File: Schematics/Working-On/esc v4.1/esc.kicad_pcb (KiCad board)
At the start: 4 copper layers, 63.5 x 38 mm, 77 parts, among them IC1 74HCT08BQ,115, IC2 74HCT08BQ,115, J1 AVR-ISP-10, J2 Conn_01x06, J3 Conn_01x06, J4 8730, J5 8730, J6 8730, J7 8730, J8 8730, U1 TLV76750DRVx, U2 ATmega328P-M, U3 DRV8300DRGER

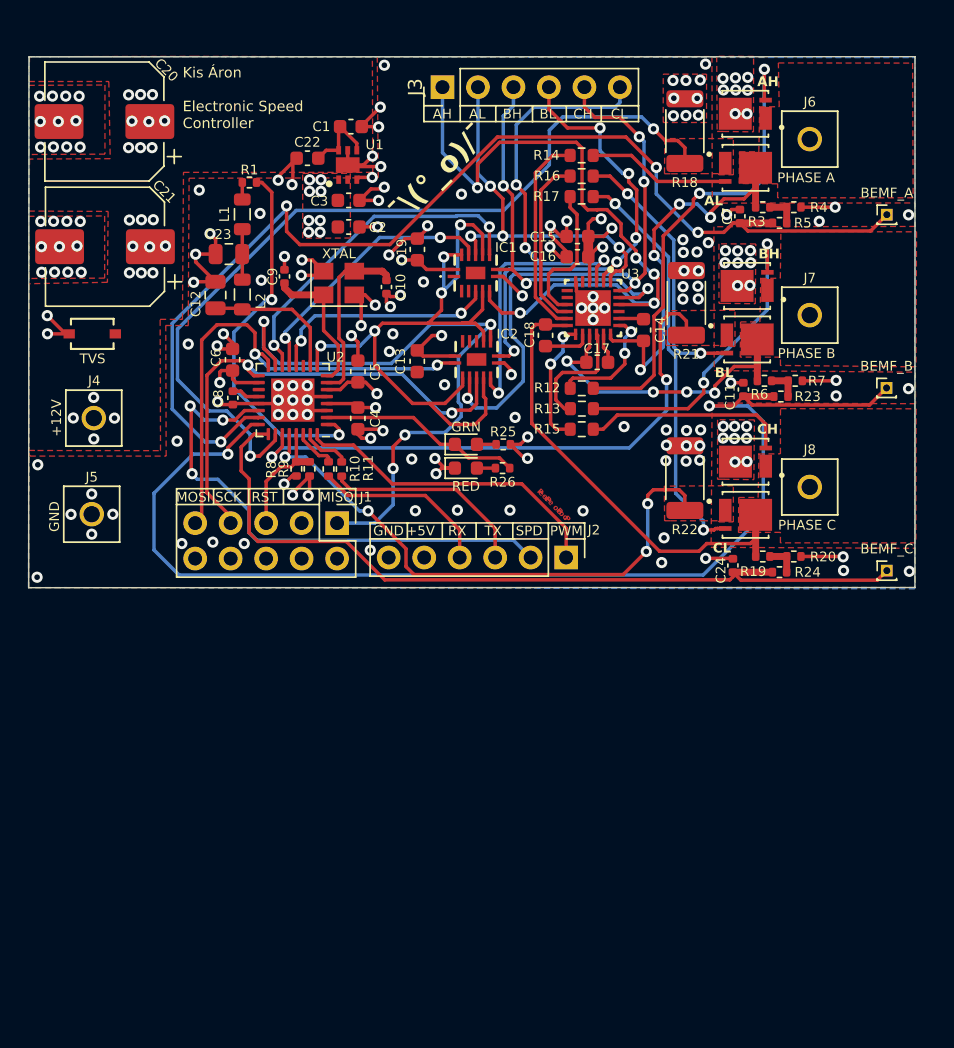
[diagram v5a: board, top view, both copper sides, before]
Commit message: Added VBUS measurment.
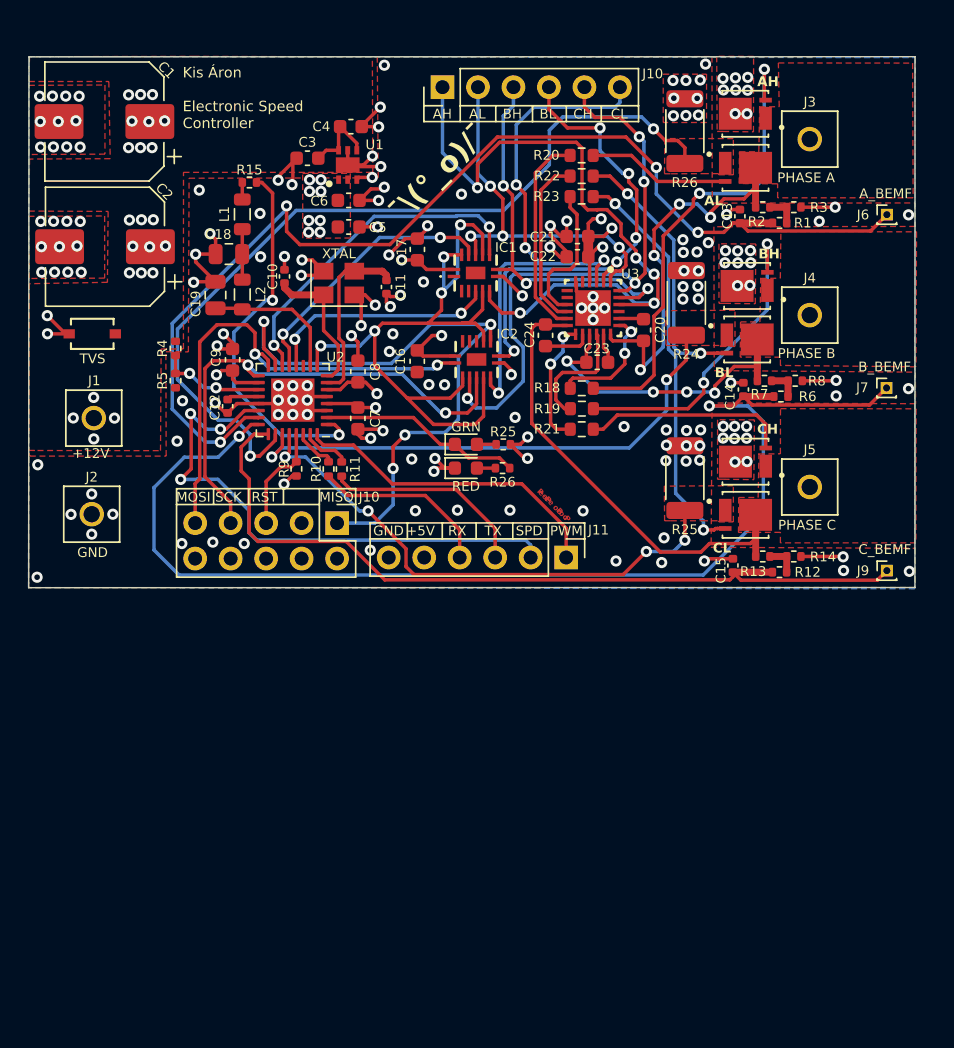
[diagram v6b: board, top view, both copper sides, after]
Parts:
- removed the R9 at (66.1, 61.5)
- added R4: 33k, Resistor_SMD:R_0402_1005Metric, F.Cu at (56.5, 52.9)
- added R5: 10k, Resistor_SMD:R_0402_1005Metric, F.Cu at (56.5, 55.2)
- moved C12 0.71 mm to (60.2, 57.0)
- renumbered C20 to C1, C9 to C10, C10 to C11, C8 to C12, C7 to C13, C11 to C14, C24 to C15, C13 to C16, C19 to C17, C23 to C18, C12 to C19, C21 to C2, C14 to C20, C15 to C21, C16 to C22, C17 to C23, C18 to C24, C22 to C3, C1 to C4, C2 to C5, C3 to C6, C4 to C7, C5 to C8, C6 to C9, J4 to J1, J1 to J10, J3 to J10, J2 to J11, J5 to J2, J6 to J3, J7 to J4, J8 to J5, BEMF_A to J6, BEMF_B to J7, BEMF_C to J9, R5 to R1, R24 to R12, R19 to R13, R20 to R14, R1 to R15, R12 to R18, R13 to R19, R3 to R2, R14 to R20, R15 to R21, R16 to R22, R17 to R23, R21 to R24, R22 to R25, R18 to R26, R4 to R3, R23 to R6, R6 to R7, R7 to R8, R8 to R9
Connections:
- U2 pad 19: unconnected-(U2-ADC6-Pad19) -> VBUS
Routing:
- net VBUS: track 0.00 -> 7.73 mm, vias 0 -> 2
- net COIL_B_CURR: track 41.4 -> 37.6 mm
- net GND: track 94.6 -> 91.9 mm
- net COIL_C_CURR: track 40.7 -> 37.9 mm
- net SPEED_REF: track 38.2 -> 39.8 mm
- net PWM_OUT: track 51.8 -> 53.1 mm
- net RST: track 8.66 -> 7.71 mm
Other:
- board text added: "A_BEMF"
- board text added: "B_BEMF"
- board text added: "C_BEMF"

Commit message: Ready to order(?)
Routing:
- net GND: track 91.9 -> 92.5 mm
- net Net-(U3-GLC): track 10.4 -> 9.89 mm
- net AH_PWM: track 49.3 -> 49.2 mm, vias 5 -> 4
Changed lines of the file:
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@@
 		(tags "capacitor")
 		(property "Reference" "C19"
-			(at 0.63 1.41 90)
+			(at 0 1.41 90)
 			(layer "F.SilkS")
 			(effects
@@
 		(tags "capacitor")
 		(property "Reference" "C5"
-			(at -2.075 -0.03 0)
+			(at -2.215 -0.01 0)
 			(layer "F.SilkS")
 			(effects
@@
 	)
 	(segment
+		(start 64.9 41.45)
+		(end 64.9 39.535)
+		(width 0.25)
+		(layer "F.Cu")
+		(net 1)
+	)
+	(segment
 		(start 103.715 42.775)
 		(end 101.27 42.775)
@@
 	)
 	(segment
-		(start 63.85 40.585)
-		(end 65.17 39.265)
-		(width 0.25)
-		(layer "F.Cu")
-		(net 1)
-	)
-	(segment
 		(start 59.37 45.07)
 		(end 59.37 46.13)
@@
 	)
 	(segment
-		(start 85.195573 48.796819)
-		(end 86.39 49.991246)
-		(width 0.25)
-		(layer "F.Cu")
-		(net 1)
-	)
-	(segment
 		(start 69.83 37.005)
 		(end 71.025 37.005)
@@
 	)
 	(segment
-		(start 85.195573 48.166818)
-		(end 85.195573 48.796819)
+		(start 57.85 47.65)
+		(end 58.31 48.11)
 		(width 0.25)
 		(layer "F.Cu")
@@
 	)
 	(segment
-		(start 69.55 59.03)
-		(end 69.55 58.665)
+		(start 85.140001 48.440001)
+		(end 85.2 48.5)
 		(width 0.25)
 		(layer "F.Cu")
@@
 	)
 	(segment
-		(start 71.675 48.965)
-		(end 71.88 49.17)
+		(start 69.55 59.03)
+		(end 69.55 58.665)
 		(width 0.25)
 		(layer "F.Cu")
@@
 	)
 	(segment
-		(start 64.84 41.16)
-		(end 64.9 41.1)
+		(start 71.675 48.965)
+		(end 71.88 49.17)
 		(width 0.25)
 		(layer "F.Cu")
@@
 	)
 	(segment
-		(start 57.84 48.11)
-		(end 57.8 48.15)
-		(width 0.25)
-		(layer "F.Cu")
-		(net 1)
-	)
-	(segment
 		(start 70.97 44.18)
 		(end 69.73 44.18)
@@
 	)
 	(segment
+		(start 64.09 41.11)
+		(end 64.09 40.345)
+		(width 0.25)
+		(layer "F.Cu")
+		(net 1)
+	)
+	(segment
 		(start 69.79 51.25)
 		(end 69.79 49.54)
@@
 	)
 	(segment
-		(start 64.645 56.83)
-		(end 64.895 56.58)
+		(start 85.2 48.801246)
+		(end 86.39 49.991246)
 		(width 0.25)
 		(layer "F.Cu")
@@
 	)
 	(segment
-		(start 59.36 48.11)
-		(end 57.84 48.11)
+		(start 64.645 56.83)
+		(end 64.895 56.58)
 		(width 0.25)
 		(layer "F.Cu")
@@
 	)
 	(segment
-		(start 85.140001 48.111246)
-		(end 85.195573 48.166818)
-		(width 0.25)
-		(layer "F.Cu")
-		(net 1)
-	)
-	(segment
 		(start 48.624 51.84)
 		(end 47.319 50.535)
@@
 	)
 	(segment
+		(start 64.09 40.345)
+		(end 65.17 39.265)
+		(width 0.25)
+		(layer "F.Cu")
+		(net 1)
+	)
+	(segment
 		(start 70.47 59.31)
 		(end 69.83 59.31)
@@
 	)
 	(segment
+		(start 85.2 48.5)
+		(end 85.2 48.801246)
+		(width 0.25)
+		(layer "F.Cu")
+		(net 1)
+	)
+	(segment
 		(start 70.07 49.05)
 		(end 69.3 49.05)
@@
 	)
 	(segment
-		(start 84.496671 43.773329)
-		(end 84.496671 44.866246)
+		(start 64.83 41.52)
+		(end 64.9 41.45)
 		(width 0.25)
 		(layer "F.Cu")
@@
 	)
 	(segment
-		(start 63.85 40.84)
-		(end 63.85 40.585)
+		(start 84.496671 43.773329)
+		(end 84.496671 44.866246)
 		(width 0.25)
 		(layer "F.Cu")
@@
 	)
 	(segment
-		(start 64.9 41.1)
-		(end 64.9 39.535)
-		(width 0.25)
-		(layer "F.Cu")
-		(net 1)
-	)
-	(segment
 		(start 79.943428 47.73)
 		(end 79.53 47.73)
@@
 		(net 1)
 	)
+	(segment
+		(start 85.140001 48.111246)
+		(end 85.140001 48.440001)
+		(width 0.25)
+		(layer "F.Cu")
+		(net 1)
+	)
+	(segment
+		(start 58.31 48.11)
+		(end 59.36 48.11)
+		(width 0.25)
+		(layer "F.Cu")
+		(net 1)
+	)
 	(via
 		(at 65.93 56.58)
@@
 	)
 	(via
-		(at 63.85 40.84)
+		(at 64.09 41.11)
 		(size 0.8)
 		(drill 0.4)
@@
 	)
 	(via
-		(at 57.8 48.15)
+		(at 57.85 47.65)
 		(size 0.8)
 		(drill 0.4)
@@
 	)
 	(via
-		(at 64.84 41.16)
+		(at 64.83 41.52)
 		(size 0.8)
 		(drill 0.4)
@@
 	)
 	(via
-		(at 62.59 46.32)
+		(at 62.65 46.52)
 		(size 0.8)
 		(drill 0.4)
@@
 	)
 	(segment
-		(start 83.532 47.228)
-		(end 83.2 47.56)
+		(start 83.57 47.53)
+		(end 83.57 49.22)
 		(width 0.25)
 		(layer "F.Cu")
@@
 	)
 	(segment
-		(start 84.746671 42.016246)
-		(end 84.746671 42.796671)
+		(start 84.091246 49.741246)
+		(end 84.538754 49.741246)
 		(width 0.25)
 		(layer "F.Cu")
@@
 	)
 	(segment
-		(start 83.2 49.057311)
-		(end 83.883935 49.741246)
+		(start 84.746671 42.016246)
+		(end 84.746671 42.796671)
 		(width 0.25)
 		(layer "F.Cu")
@@
 	)
 	(segment
-		(start 84.746997 47.228)
-		(end 83.532 47.228)
+		(start 85.24 43.29)
+		(end 85.24 46.89)
 		(width 0.25)
 		(layer "F.Cu")
@@
 	)
 	(segment
-		(start 83.2 47.56)
-		(end 83.2 49.057311)
+		(start 85.24 46.89)
+		(end 84.75 47.38)
 		(width 0.25)
 		(layer "F.Cu")
@@
 	)
 	(segment
-		(start 85.24 46.734997)
-		(end 84.746997 47.228)
+		(start 83.57 49.22)
+		(end 84.091246 49.741246)
 		(width 0.25)
 		(layer "F.Cu")
@@
 	)
 	(segment
-		(start 83.883935 49.741246)
-		(end 84.538754 49.741246)
+		(start 84.75 47.38)
+		(end 83.72 47.38)
 		(width 0.25)
 		(layer "F.Cu")
@@
 	)
 	(segment
-		(start 85.24 43.29)
-		(end 85.24 46.734997)
+		(start 83.72 47.38)
+		(end 83.57 47.53)
 		(width 0.25)
 		(layer "F.Cu")
@@
 	)
 	(segment
-		(start 90.76 49.64)
-		(end 91.029034 49.370966)
-		(width 0.25)
-		(layer "F.Cu")
-		(net 46)
-	)
-	(segment
 		(start 81.17 50.34)
 		(end 79.88 50.34)
@@
 	)
 	(segment
-		(start 91.029034 47.830068)
-		(end 90.758966 47.56)
-		(width 0.25)
-		(layer "F.Cu")
-		(net 46)
-	)
-	(segment
 		(start 86.687932 42.96)
 		(end 86.699932 42.948)
@@
 	)
 	(segment
-		(start 91.029034 49.370966)
-		(end 91.029034 47.830068)
-		(width 0.25)
-		(layer "F.Cu")
-		(net 46)
-	)
-	(segment
 		(start 86 42.96)
 		(end 86.687932 42.96)
@@
 	)
 	(via
-		(at 90.758966 47.56)
-		(size 0.8)
-		(drill 0.4)
-		(layers "F.Cu" "B.Cu")
-		(net 46)
-	)
-	(via
 		(at 90.76 49.64)
 		(size 0.8)
@@
 	)
 	(segment
+		(start 90.962 47.917034)
+		(end 90.962 49.438)
+		(width 0.25)
+		(layer "B.Cu")
+		(net 46)
+	)
+	(segment
+		(start 90.962 49.438)
+		(end 90.76 49.64)
+		(width 0.25)
+		(layer "B.Cu")
+		(net 46)
+	)
+	(segment
 		(start 89.374774 49.64)
 		(end 90.76 49.64)
@@
 	)
 	(segment
-		(start 90.758966 47.56)
-		(end 90.604966 47.56)
-		(width 0.25)
-		(layer "B.Cu")
-		(net 46)
-	)
-	(segment
 		(start 81.17 50.34)
 		(end 81.612568 50.34)
@@
 	)
 	(segment
-		(start 90.604966 47.56)
-		(end 89.454966 46.41)
+		(start 89.454966 46.41)
+		(end 90.962 47.917034)
 		(width 0.25)
 		(layer "B.Cu")
@@
 	)
 	(segment
-		(start 59.715652 58.666546)
+		(start 59.47 58.666546)
 		(end 60.103454 58.666546)
 		(width 0.25)
@@
 	)
 	(via
-		(at 59.715652 58.666546)
+		(at 59.47 58.666546)
 		(size 0.8)
 		(drill 0.4)
@@
 	)
 	(segment
-		(start 58.694546 58.666546)
-		(end 57.578 57.55)
+		(start 56.86925 62.25925)
+		(end 58.04075 62.25925)
 		(width 0.25)
 		(layer "B.Cu")
@@
 	)
 	(segment
-		(start 56.86925 62.25925)
-		(end 58.04075 62.25925)
+		(start 58.694546 58.666546)
+		(end 57.578 57.55)
 		(width 0.25)
 		(layer "B.Cu")
@@
 	)
 	(segment
-		(start 59.715652 58.666546)
+		(start 59.47 58.666546)
 		(end 58.694546 58.666546)
 		(width 0.25)

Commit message: Ready to order.
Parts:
- added C25: 100n, Capacitor_SMD:C_0402_1005Metric, F.Cu at (54.5, 55.2)
- J6, J7: footprint Connector_PinHeader_1.00mm:PinHeader_1x01_P1.00mm_Vertical -> Connector_PinHeader_2.54mm:PinHeader_1x01_P2.54mm_Vertical
- J8: renamed from J9; footprint Connector_PinHeader_1.00mm:PinHeader_1x01_P1.00mm_Vertical -> Connector_PinHeader_2.54mm:PinHeader_1x01_P2.54mm_Vertical
- moved J8 1.00 mm to (106.5, 68.3)
- moved J6 0.91 mm to (106.5, 43.2)
- moved J7 0.91 mm to (106.5, 55.6)
- moved R9 0.49 mm to (65.6, 61.6)
- moved J4 0.42 mm to (102.0, 50.1)
- moved J5 0.30 mm to (101.9, 62.5)
- moved R10 0.12 mm to (67.5, 61.4)
- moved R11 0.12 mm to (68.4, 61.4)
- turned C16 to -90 degrees
- turned C17 to 90 degrees
- renumbered J10 to J9
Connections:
- C16 pad 1: GND -> +5V
- C16 pad 2: +5V -> GND
- C17 pad 1: GND -> +5V
- C17 pad 2: +5V -> GND
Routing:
- net GND: track 92.5 -> 103.0 mm, vias 145 -> 138
- net COIL_A_BEMF: track 81.5 -> 79.2 mm
- net VBUS: track 7.73 -> 9.73 mm
- net +5V: track 24.9 -> 23.0 mm
- net PWM_OUT: track 53.1 -> 54.8 mm
- net CL_PWM: track 39.6 -> 38.2 mm
- net Net-(U3-GHC): track 9.11 -> 10.5 mm
- net AH_PWM: track 49.2 -> 48.0 mm
- net COIL_C_BEMF: track 59.5 -> 58.5 mm
- net COIL_A_CURR: track 60.8 -> 61.6 mm
- net +12V: track 14.2 -> 13.5 mm
- net BL: track 46.5 -> 45.9 mm
- net Net-(U2-PD1): track 3.50 -> 4.04 mm
- net COIL_C_CURR: track 37.9 -> 38.4 mm
- net CH_PWM: track 42.3 -> 41.8 mm
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- added copper zone on In2.Cu, net COIL_A
- added copper zone on In2.Cu, net COIL_B
- added copper zone on In2.Cu, net COIL_C
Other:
- board size 63.5 x 38 mm -> 62.5 x 38 mm
- board text added: "PeePee PooPoo"
- board text removed: "P P P P"
- board text removed: "ee"
- board text removed: "oo"
